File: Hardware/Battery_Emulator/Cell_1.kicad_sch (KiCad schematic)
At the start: 27 parts, among them Q1 IRFB7545PBF, SW1 Jumper, SW2 Jumper, U1 MCP4651T-103E_ST, U2 ISO1640BDR, U7 LM317_TO-220, U8 MCP6001UT-I/OT, U9 KA78M05_TO252

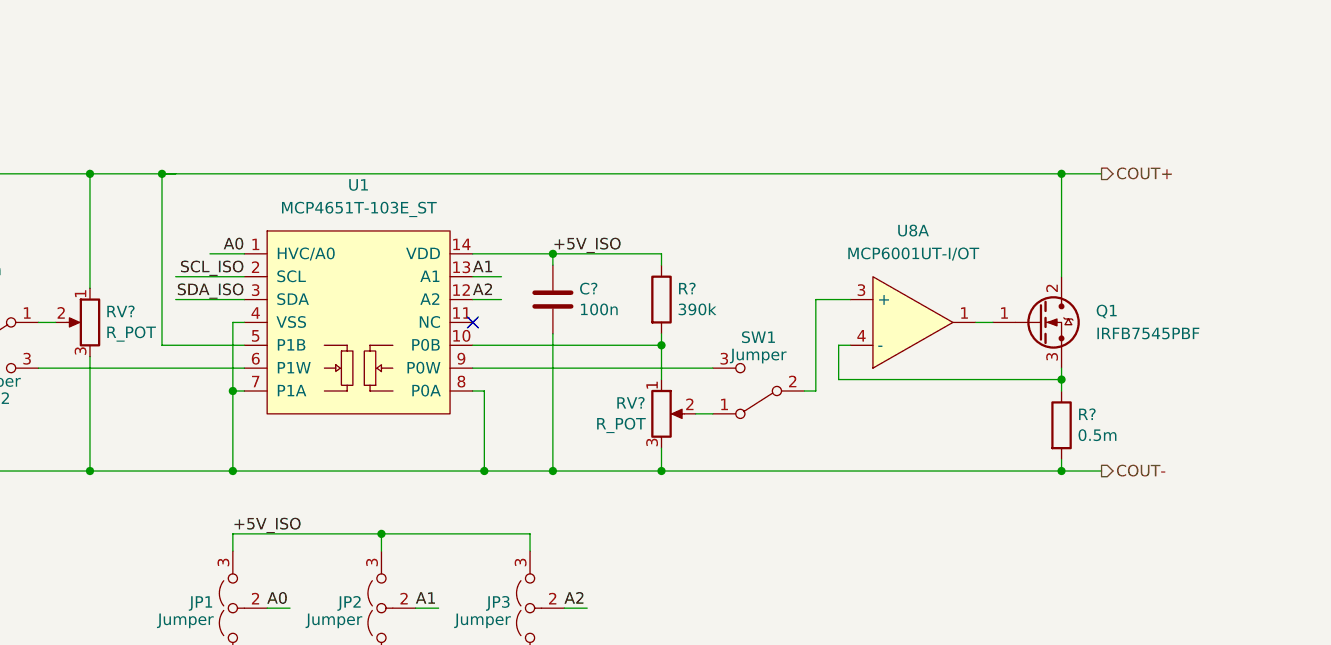
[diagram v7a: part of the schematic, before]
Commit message: Update PCB
Made traces a lot larger to pass more current.
Added resistor to gate of current sink MOSFET.
Made the gerber files and ordered it at SMD lab.
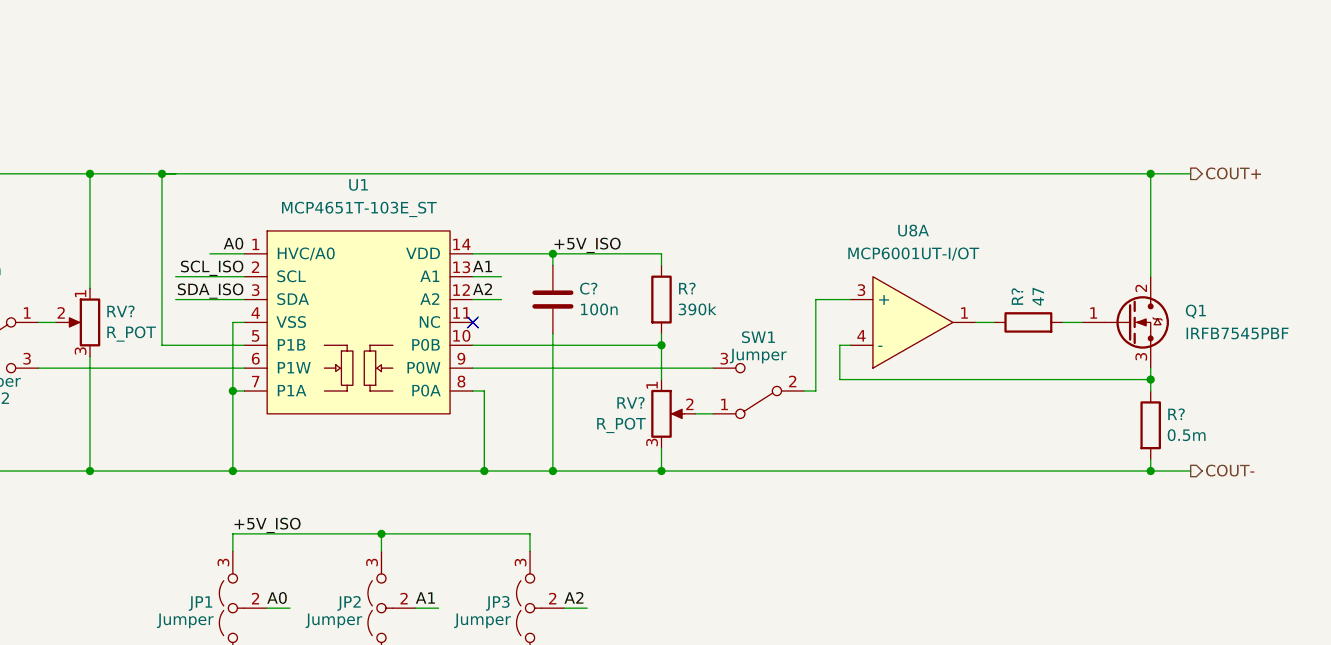
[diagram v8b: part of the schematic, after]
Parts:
- added R?: 47, Resistor_SMD:R_0805_2012Metric, symbol Device:R
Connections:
- net at U8.1: now also R?.1; no longer Q1.1
- new net: Q1.1, R?.2
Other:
- moved on the sheet: Q1, R?
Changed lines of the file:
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@@
   (junction (at 116.84 66.675) (diameter 0) (color 0 0 0 0)
   )
-  (junction (at 183.261 141.224) (diameter 0) (color 0 0 0 0)
+  (junction (at 193.167 141.224) (diameter 0) (color 0 0 0 0)
   )
   (junction (at 41.91 52.07) (diameter 0) (color 0 0 0 0)
@@
   (junction (at 35.941 108.204) (diameter 0) (color 0 0 0 0)
   )
-  (junction (at 183.261 131.064) (diameter 0) (color 0 0 0 0)
-  )
-  (junction (at 183.261 108.204) (diameter 0) (color 0 0 0 0)
+  (junction (at 193.167 131.064) (diameter 0) (color 0 0 0 0)
+  )
+  (junction (at 193.167 108.204) (diameter 0) (color 0 0 0 0)
   )
   (junction (at 119.126 141.224) (diameter 0) (color 0 0 0 0)
@@
     (stroke (width 1) (type default))
   )
+  (wire (pts (xy 83.312 108.204) (xy 193.167 108.204))
+    (stroke (width 1) (type default))
+  )
   (wire (pts (xy 74.93 80.645) (xy 83.185 80.645))
     (stroke (width 0) (type default))
@@
     (stroke (width 0) (type default))
   )
-  (wire (pts (xy 183.261 141.224) (xy 187.706 141.224))
-    (stroke (width 1) (type default))
-  )
-  (wire (pts (xy 183.261 119.634) (xy 183.261 108.204))
-    (stroke (width 1) (type default))
-  )
-  (wire (pts (xy 183.261 129.794) (xy 183.261 131.064))
+  (wire (pts (xy 193.167 141.224) (xy 197.612 141.224))
+    (stroke (width 1) (type default))
+  )
+  (wire (pts (xy 193.167 119.634) (xy 193.167 108.204))
+    (stroke (width 1) (type default))
+  )
+  (wire (pts (xy 193.167 129.794) (xy 193.167 131.064))
     (stroke (width 1) (type default))
   )
@@
     (stroke (width 1) (type default))
   )
-  (wire (pts (xy 159.766 127.254) (xy 158.496 127.254))
+  (wire (pts (xy 158.623 127.254) (xy 159.766 127.254))
     (stroke (width 0) (type default))
   )
@@
     (stroke (width 1) (type default))
   )
-  (wire (pts (xy 183.261 131.064) (xy 183.261 132.334))
+  (wire (pts (xy 193.167 131.064) (xy 193.167 132.334))
     (stroke (width 1) (type default))
   )
@@
     (stroke (width 0) (type default))
   )
-  (wire (pts (xy 138.811 141.224) (xy 183.261 141.224))
-    (stroke (width 1) (type default))
-  )
   (wire (pts (xy 137.795 65.405) (xy 137.795 66.675))
     (stroke (width 0) (type default))
@@
     (stroke (width 0) (type default))
   )
-  (wire (pts (xy 173.736 124.714) (xy 175.641 124.714))
+  (wire (pts (xy 173.736 124.714) (xy 175.768 124.714))
     (stroke (width 0) (type default))
   )
@@
     (stroke (width 0) (type default))
   )
-  (wire (pts (xy 183.261 139.954) (xy 183.261 141.224))
+  (wire (pts (xy 193.167 139.954) (xy 193.167 141.224))
     (stroke (width 1) (type default))
   )
@@
     (stroke (width 0) (type default))
   )
-  (wire (pts (xy 158.496 127.254) (xy 158.496 131.064))
+  (wire (pts (xy 158.623 127.254) (xy 158.623 131.064))
     (stroke (width 0) (type default))
   )
@@
     (stroke (width 0) (type default))
   )
+  (wire (pts (xy 138.811 141.224) (xy 193.167 141.224))
+    (stroke (width 1) (type default))
+  )
   (wire (pts (xy 27.051 141.224) (xy 35.941 141.224))
     (stroke (width 1) (type default))
   )
-  (wire (pts (xy 183.261 108.204) (xy 187.706 108.204))
+  (wire (pts (xy 193.167 108.204) (xy 197.612 108.204))
     (stroke (width 1) (type default))
   )
@@
     (stroke (width 0) (type default))
   )
-  (wire (pts (xy 83.312 108.204) (xy 183.261 108.204))
-    (stroke (width 1) (type default))
+  (wire (pts (xy 183.388 124.714) (xy 185.547 124.714))
+    (stroke (width 0) (type default))
   )
   (wire (pts (xy 81.28 60.96) (xy 81.28 66.675))
@@
     (stroke (width 0) (type default))
   )
-  (wire (pts (xy 158.496 131.064) (xy 183.261 131.064))
+  (wire (pts (xy 158.623 131.064) (xy 193.167 131.064))
     (stroke (width 0) (type default))
   )
@@
     (effects (font (size 1.27 1.27)) (justify right))
   )
-  (hierarchical_label "COUT+" (shape output) (at 187.706 108.204 0) (fields_autoplaced)
+  (hierarchical_label "COUT+" (shape output) (at 197.612 108.204 0) (fields_autoplaced)
     (effects (font (size 1.27 1.27)) (justify left))
   )
-  (hierarchical_label "COUT-" (shape output) (at 187.706 141.224 0) (fields_autoplaced)
+  (hierarchical_label "COUT-" (shape output) (at 197.612 141.224 0) (fields_autoplaced)
     (effects (font (size 1.27 1.27)) (justify left))
   )
@@
         (path "/bb7641ff-0dfd-4f4a-b3be-57afbbb9fdac/86a0f187-fc20-4f8c-b621-2752c8234446"
           (reference "RV4") (unit 1)
+        )
+      )
+    )
+  )
+  (symbol (lib_id "Device:R") (at 179.578 124.714 90) (unit 1)
+    (in_bom yes) (on_board yes) (dnp no)
+    (property "Reference" "R?" (at 178.4096 122.936 0)
+      (effects (font (size 1.27 1.27)) (justify left))
+    )
+    (property "Value" "47" (at 180.721 122.936 0)
+      (effects (font (size 1.27 1.27)) (justify left))
+    )
+    (property "Footprint" "Resistor_SMD:R_0805_2012Metric" (at 179.578 126.492 90)
+      (effects (font (size 1.27 1.27)) hide)
+    )
+    (property "Datasheet" "https://nl.mouser.com/ProductDetail/Ohmite/PCS2512FR0050ET?qs=sGAEpiMZZMtlleCFQhR%2FzRH%2FPnzm6Qg0HsYmtkKDwHfIXEJ4ch5rIQ%3D%3D" (at 179.578 124.714 0)
+      (effects (font (size 1.27 1.27)) hide)
+    )
+    (pin "1")
+    (pin "2")
+    (instances
+      (project "Battery_Emulator"
+        (path "/bb7641ff-0dfd-4f4a-b3be-57afbbb9fdac"
+          (reference "R?") (unit 1)
+        )
+        (path "/bb7641ff-0dfd-4f4a-b3be-57afbbb9fdac/86a0f187-fc20-4f8c-b621-2752c8234446"
+          (reference "R7") (unit 1)
         )
       )
@@
     )
   )
-  (symbol (lib_id "Device:R") (at 183.261 136.144 0) (unit 1)
-    (in_bom yes) (on_board yes) (dnp no)
-    (property "Reference" "R?" (at 185.039 134.9756 0)
-      (effects (font (size 1.27 1.27)) (justify left))
-    )
-    (property "Value" "0.5m" (at 185.039 137.287 0)
-      (effects (font (size 1.27 1.27)) (justify left))
-    )
-    (property "Footprint" "Resistor_SMD:R_2512_6332Metric" (at 181.483 136.144 90)
-      (effects (font (size 1.27 1.27)) hide)
-    )
-    (property "Datasheet" "https://nl.mouser.com/ProductDetail/Ohmite/PCS2512FR0050ET?qs=sGAEpiMZZMtlleCFQhR%2FzRH%2FPnzm6Qg0HsYmtkKDwHfIXEJ4ch5rIQ%3D%3D" (at 183.261 136.144 0)
+  (symbol (lib_id "Device:R") (at 193.167 136.144 0) (unit 1)
+    (in_bom yes) (on_board yes) (dnp no)
+    (property "Reference" "R?" (at 194.945 134.9756 0)
+      (effects (font (size 1.27 1.27)) (justify left))
+    )
+    (property "Value" "0.5m" (at 194.945 137.287 0)
+      (effects (font (size 1.27 1.27)) (justify left))
+    )
+    (property "Footprint" "Resistor_SMD:R_2512_6332Metric" (at 191.389 136.144 90)
+      (effects (font (size 1.27 1.27)) hide)
+    )
+    (property "Datasheet" "https://nl.mouser.com/ProductDetail/Ohmite/PCS2512FR0050ET?qs=sGAEpiMZZMtlleCFQhR%2FzRH%2FPnzm6Qg0HsYmtkKDwHfIXEJ4ch5rIQ%3D%3D" (at 193.167 136.144 0)
       (effects (font (size 1.27 1.27)) hide)
     )
@@
     )
   )
-  (symbol (lib_id "PR7 Custom:IRFB7545PBF") (at 183.261 124.714 0) (unit 1)
+  (symbol (lib_id "PR7 Custom:IRFB7545PBF") (at 193.167 124.714 0) (unit 1)
     (in_bom yes) (on_board yes) (dnp no) (fields_autoplaced)
-    (property "Reference" "Q1" (at 187.071 123.444 0)
-      (effects (font (size 1.27 1.27)) (justify left))
-    )
-    (property "Value" "IRFB7545PBF" (at 187.071 125.984 0)
-      (effects (font (size 1.27 1.27)) (justify left))
-    )
-    (property "Footprint" "Package_TO_SOT_THT:TO-220-3_Horizontal_TabUp" (at 183.261 124.714 0)
-      (effects (font (size 1.27 1.27)) hide)
-    )
-    (property "Datasheet" "https://nl.mouser.com/ProductDetail/Infineon-Technologies/IRFB7545PBF?qs=a7rcPCEf1Q%252BjvB7f7k7q9g%3D%3D" (at 183.261 124.714 0)
-      (effects (font (size 1.27 1.27)) hide)
-    )
+    (property "Reference" "Q1" (at 196.977 123.444 0)
+      (effects (font (size 1.27 1.27)) (justify left))
+    )
+    (property "Value" "IRFB7545PBF" (at 196.977 125.984 0)
+      (effects (font (size 1.27 1.27)) (justify left))
+    )
+    (property "Footprint" "Package_TO_SOT_THT:TO-220-3_Horizontal_TabUp" (at 193.167 124.714 0)
+      (effects (font (size 1.27 1.27)) hide)
+    )
+    (property "Datasheet" "https://nl.mouser.com/ProductDetail/Infineon-Technologies/IRFB7545PBF?qs=a7rcPCEf1Q%252BjvB7f7k7q9g%3D%3D" (at 193.167 124.714 0)
+      (effects (font (size 1.27 1.27)) hide)
+    )
